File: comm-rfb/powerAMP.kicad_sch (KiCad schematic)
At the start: 14 parts

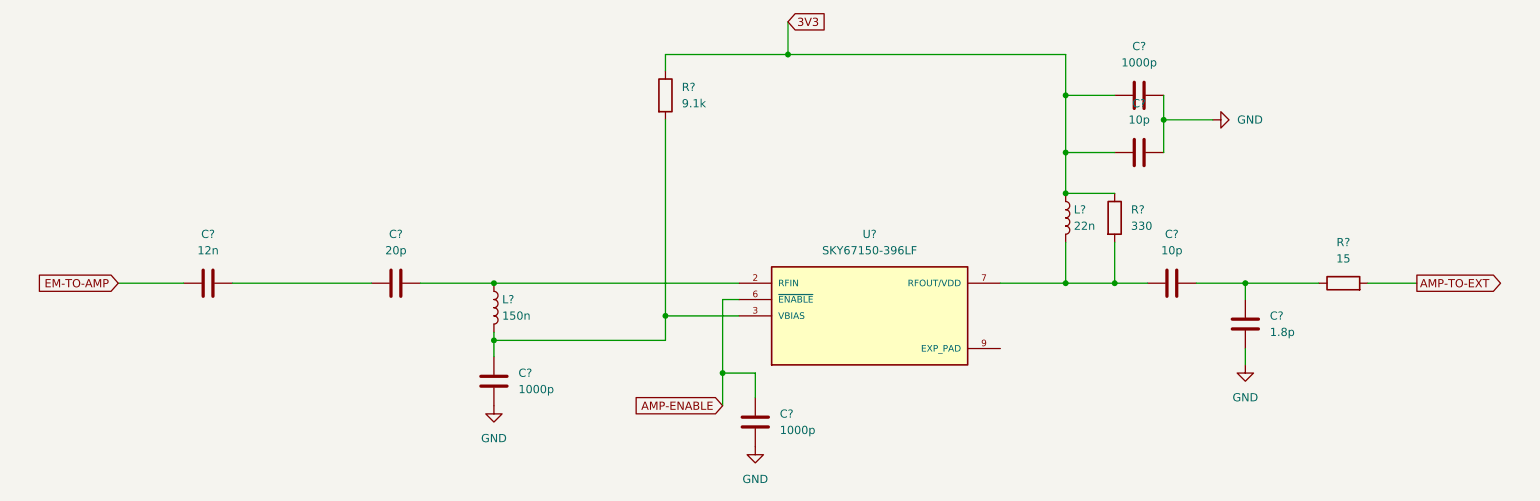
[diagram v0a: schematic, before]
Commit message: comm-rfb: reformat main schematic page
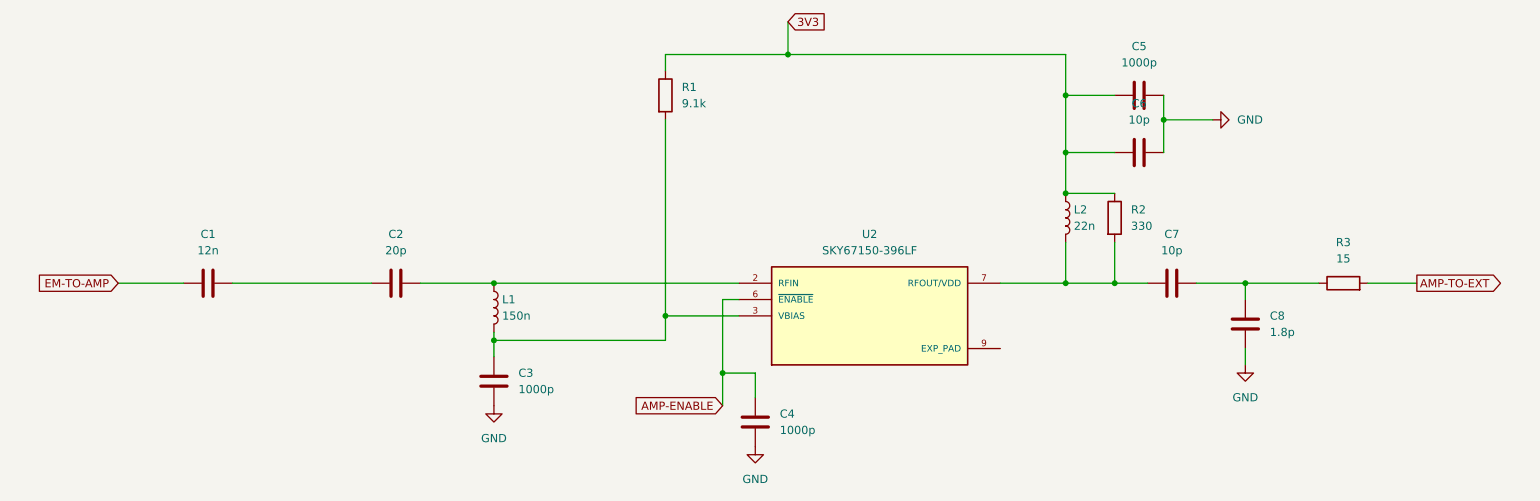
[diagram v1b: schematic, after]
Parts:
- gave numbers to parts that had none: 14
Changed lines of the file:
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@@
   (symbol (lib_id "power:GND") (at 107.95 119.38 0) (unit 1)
     (in_bom yes) (on_board yes) (fields_autoplaced)
-    (property "Reference" "#PWR?" (id 0) (at 107.95 125.73 0)
+    (property "Reference" "#PWR09" (id 0) (at 107.95 125.73 0)
       (effects (font (size 1.27 1.27)) hide)
     )
@@
   (symbol (lib_id "Device:C") (at 224.79 106.68 0) (unit 1)
     (in_bom yes) (on_board yes) (fields_autoplaced)
-    (property "Reference" "C?" (id 0) (at 228.6 105.4099 0)
+    (property "Reference" "C8" (id 0) (at 228.6 105.4099 0)
       (effects (font (size 1.27 1.27)) (justify left))
     )
@@
   (symbol (lib_id "Device:C") (at 107.95 115.57 0) (unit 1)
     (in_bom yes) (on_board yes) (fields_autoplaced)
-    (property "Reference" "C?" (id 0) (at 111.76 114.2999 0)
+    (property "Reference" "C3" (id 0) (at 111.76 114.2999 0)
       (effects (font (size 1.27 1.27)) (justify left))
     )
@@
   (symbol (lib_id "power:GND") (at 219.71 74.93 90) (unit 1)
     (in_bom yes) (on_board yes) (fields_autoplaced)
-    (property "Reference" "#PWR?" (id 0) (at 226.06 74.93 0)
+    (property "Reference" "#PWR011" (id 0) (at 226.06 74.93 0)
       (effects (font (size 1.27 1.27)) hide)
     )
@@
   (symbol (lib_id "Device:C") (at 213.36 100.33 90) (unit 1)
     (in_bom yes) (on_board yes) (fields_autoplaced)
-    (property "Reference" "C?" (id 0) (at 213.36 92.71 90))
+    (property "Reference" "C7" (id 0) (at 213.36 92.71 90))
     (property "Value" "10p" (id 1) (at 213.36 95.25 90))
     (property "Footprint" "" (id 2) (at 217.17 99.3648 0)
@@
   (symbol (lib_id "Device:L") (at 107.95 104.14 0) (unit 1)
     (in_bom yes) (on_board yes) (fields_autoplaced)
-    (property "Reference" "L?" (id 0) (at 109.22 102.8699 0)
+    (property "Reference" "L1" (id 0) (at 109.22 102.8699 0)
       (effects (font (size 1.27 1.27)) (justify left))
     )
@@
   (symbol (lib_id "Device:C") (at 92.71 100.33 90) (unit 1)
     (in_bom yes) (on_board yes) (fields_autoplaced)
-    (property "Reference" "C?" (id 0) (at 92.71 92.71 90))
+    (property "Reference" "C2" (id 0) (at 92.71 92.71 90))
     (property "Value" "20p" (id 1) (at 92.71 95.25 90))
     (property "Footprint" "" (id 2) (at 96.52 99.3648 0)
@@
   (symbol (lib_id "Device:C") (at 208.28 71.12 90) (unit 1)
     (in_bom yes) (on_board yes) (fields_autoplaced)
-    (property "Reference" "C?" (id 0) (at 208.28 63.5 90))
+    (property "Reference" "C5" (id 0) (at 208.28 63.5 90))
     (property "Value" "1000p" (id 1) (at 208.28 66.04 90))
     (property "Footprint" "" (id 2) (at 212.09 70.1548 0)
@@
   (symbol (lib_id "Device:R") (at 240.03 100.33 90) (unit 1)
     (in_bom yes) (on_board yes) (fields_autoplaced)
-    (property "Reference" "R?" (id 0) (at 240.03 93.98 90))
+    (property "Reference" "R3" (id 0) (at 240.03 93.98 90))
     (property "Value" "15" (id 1) (at 240.03 96.52 90))
     (property "Footprint" "" (id 2) (at 240.03 102.108 90)
@@
   (symbol (lib_id "Device:R") (at 204.47 90.17 0) (unit 1)
     (in_bom yes) (on_board yes) (fields_autoplaced)
-    (property "Reference" "R?" (id 0) (at 207.01 88.8999 0)
+    (property "Reference" "R2" (id 0) (at 207.01 88.8999 0)
       (effects (font (size 1.27 1.27)) (justify left))
     )
@@
   (symbol (lib_id "Device:L") (at 196.85 90.17 0) (unit 1)
     (in_bom yes) (on_board yes) (fields_autoplaced)
-    (property "Reference" "L?" (id 0) (at 198.12 88.8999 0)
+    (property "Reference" "L2" (id 0) (at 198.12 88.8999 0)
       (effects (font (size 1.27 1.27)) (justify left))
     )
@@
   (symbol (lib_id "power:GND") (at 224.79 113.03 0) (unit 1)
     (in_bom yes) (on_board yes) (fields_autoplaced)
-    (property "Reference" "#PWR?" (id 0) (at 224.79 119.38 0)
+    (property "Reference" "#PWR012" (id 0) (at 224.79 119.38 0)
       (effects (font (size 1.27 1.27)) hide)
     )
@@
   (symbol (lib_id "Device:C") (at 148.59 121.92 0) (unit 1)
     (in_bom yes) (on_board yes) (fields_autoplaced)
-    (property "Reference" "C?" (id 0) (at 152.4 120.6499 0)
+    (property "Reference" "C4" (id 0) (at 152.4 120.6499 0)
       (effects (font (size 1.27 1.27)) (justify left))
     )
@@
   (symbol (lib_id "power:GND") (at 148.59 125.73 0) (unit 1)
     (in_bom yes) (on_board yes) (fields_autoplaced)
-    (property "Reference" "#PWR?" (id 0) (at 148.59 132.08 0)
+    (property "Reference" "#PWR010" (id 0) (at 148.59 132.08 0)
       (effects (font (size 1.27 1.27)) hide)
     )
@@
   (symbol (lib_id "Device:C") (at 63.5 100.33 270) (unit 1)
     (in_bom yes) (on_board yes) (fields_autoplaced)
-    (property "Reference" "C?" (id 0) (at 63.5 92.71 90))
+    (property "Reference" "C1" (id 0) (at 63.5 92.71 90))
     (property "Value" "12n" (id 1) (at 63.5 95.25 90))
     (property "Footprint" "" (id 2) (at 59.69 101.2952 0)
@@
   (symbol (lib_id "Device:R") (at 134.62 71.12 0) (unit 1)
     (in_bom yes) (on_board yes) (fields_autoplaced)
-    (property "Reference" "R?" (id 0) (at 137.16 69.8499 0)
+    (property "Reference" "R1" (id 0) (at 137.16 69.8499 0)
       (effects (font (size 1.27 1.27)) (justify left))
     )
@@
   (symbol (lib_id "SKY67150-396LF:SKY67150-396LF") (at 166.37 105.41 0) (unit 1)
     (in_bom yes) (on_board yes) (fields_autoplaced)
-    (property "Reference" "U?" (id 0) (at 166.37 92.71 0))
+    (property "Reference" "U2" (id 0) (at 166.37 92.71 0))
     (property "Value" "SKY67150-396LF" (id 1) (at 166.37 95.25 0))
     (property "Footprint" "SON50P200X200X80-9N" (id 2) (at 166.37 105.41 0)
@@
   (symbol (lib_id "Device:C") (at 208.28 80.01 90) (unit 1)
     (in_bom yes) (on_board yes) (fields_autoplaced)
-    (property "Reference" "C?" (id 0) (at 208.28 72.39 90))
+    (property "Reference" "C6" (id 0) (at 208.28 72.39 90))
     (property "Value" "10p" (id 1) (at 208.28 74.93 90))
     (property "Footprint" "" (id 2) (at 212.09 79.0448 0)
